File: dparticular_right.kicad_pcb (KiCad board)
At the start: 2 copper layers, 185.7 x 157.2 mm, 51 parts, among them J1 To Left Hand, SW1:10 Key_Ins, SW1:11 Key_Prnt, SW2:10 Key_F7, SW2:11 Key_F8, SW2:12 Key_F9, SW2:13 Key_F10, SW2:14 Key_F11, SW2:15 Key_F12, SW2:16 Key_Del, SW3:10 Key_7, SW3:11 Key_8, SW3:12 Key_9, SW3:13 Key_0, SW3:14 Key_Hyph, SW3:15 Key_Eql, SW3:16 Key_Bksp, SW3:9 Key_6, SW4:10 Key_U, SW4:11 Key_I, SW4:12 Key_O, SW4:13 Key_P, SW4:14 Key_LBrk, SW4:15 Key_RBrk, SW4:16 Key_BkSl, SW4:9 Key_Y, SW5:10 Key_J, SW5:11 Key_K, SW5:12 Key_L, SW5:13 Key_Semi, SW5:14 Key_Quot, SW5:16 Key_Entr, SW5:9 Key_H, SW6:10 Key_M, SW6:11 Key_Coma, SW6:12 Key_Per, SW6:13 Key_Slsh, SW6:14 Key_RShft, SW6:9 Key_N, SW7:11 Key_RAlt, SW7:12 Key_RWin, SW7:13 Key_Menu, SW7:14 Key_RCtrl, SW7:9 Key_RSpc, U1 MCP23018

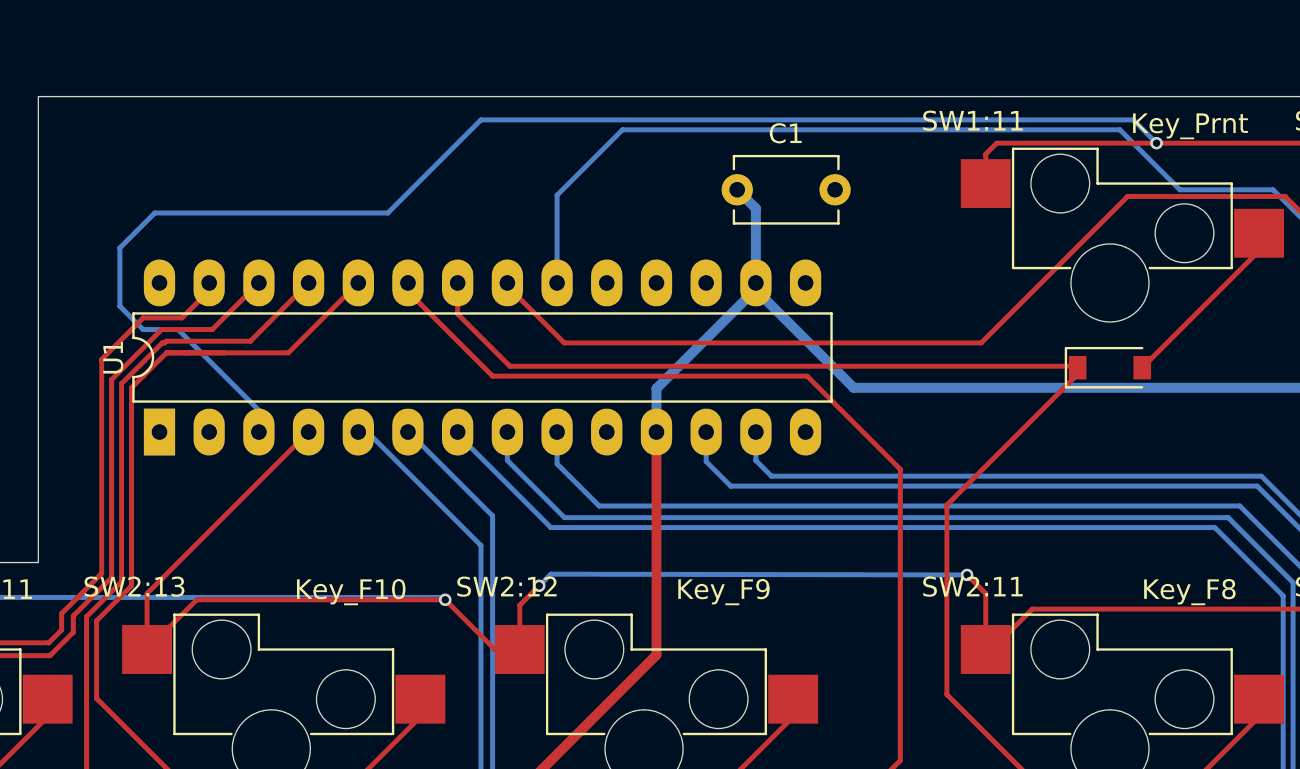
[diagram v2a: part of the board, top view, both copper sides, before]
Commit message: Righ Hand PCB: improved ground plane coverage
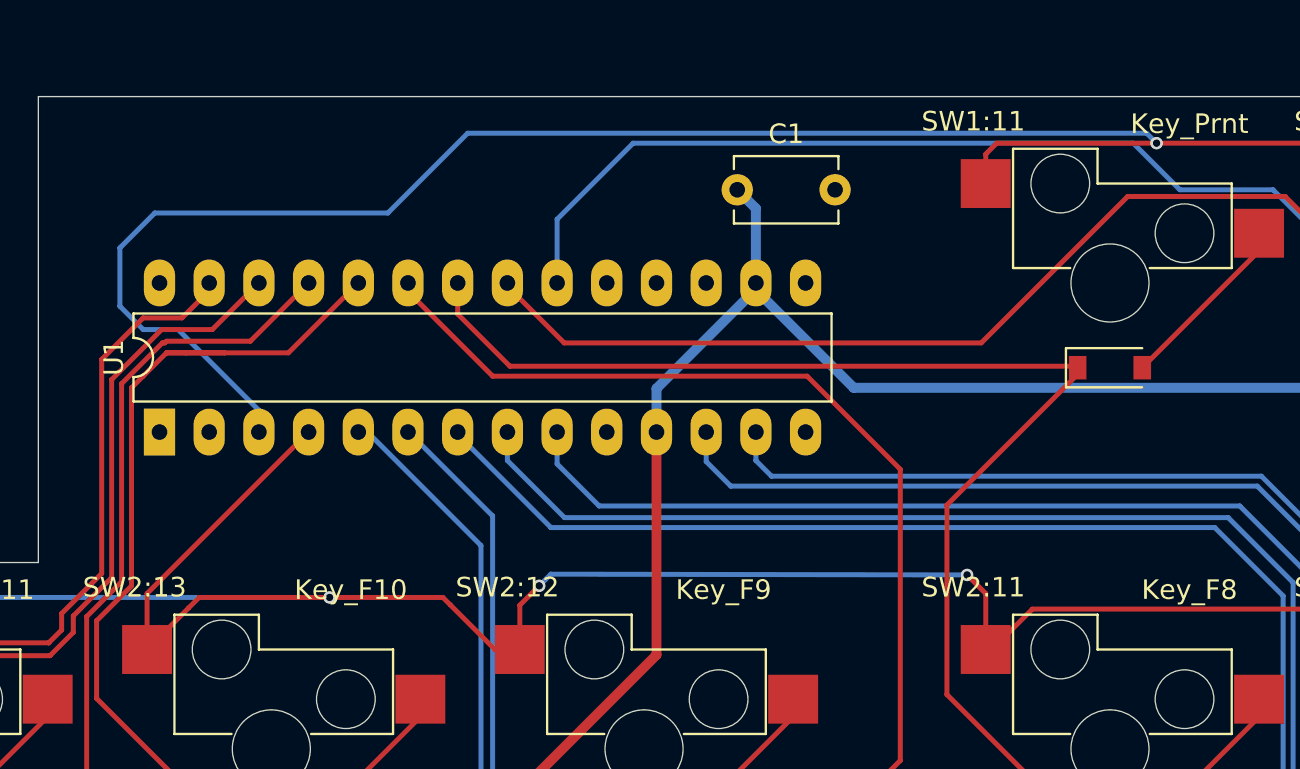
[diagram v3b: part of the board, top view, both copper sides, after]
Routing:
- net /ROW2: track 203.1 -> 197.2 mm
- net /COL9: track 254.1 -> 252.8 mm
- net /ROW1: track 91.2 -> 90.7 mm
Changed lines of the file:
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@@
     (thickness 1.6)
     (drawings 50)
-    (tracks 793)
+    (tracks 797)
     (zones 0)
     (modules 51)
@@
   (segment (start 151.37225 26.19375) (end 167.79875 26.19375) (width 0.254) (layer F.Cu) (net 11))
   (via (at 159.543852 26.19374) (size 0.635) (drill 0.381) (layers F.Cu B.Cu) (net 11))
-  (segment (start 158.353248 25.003136) (end 159.543852 26.19374) (width 0.254) (layer B.Cu) (net 11))
-  (segment (start 125.015552 25.003136) (end 158.353248 25.003136) (width 0.254) (layer B.Cu) (net 11))
-  (segment (start 120.25625 29.762438) (end 125.015552 25.003136) (width 0.254) (layer B.Cu) (net 11))
-  (segment (start 108.343622 29.762438) (end 120.25625 29.762438) (width 0.254) (layer B.Cu) (net 11))
-  (segment (start 113.665 40.9575) (end 113.665 39.846312) (width 0.254) (layer B.Cu) (net 11))
-  (segment (start 109.53744 35.718752) (end 107.751504 35.718752) (width 0.254) (layer B.Cu) (net 11))
-  (segment (start 113.665 39.846312) (end 109.53744 35.718752) (width 0.254) (layer B.Cu) (net 11))
-  (segment (start 107.751504 35.718752) (end 106.56088 34.528128) (width 0.254) (layer B.Cu) (net 11))
-  (segment (start 106.56088 34.528128) (end 106.56088 31.54518) (width 0.254) (layer B.Cu) (net 11))
-  (segment (start 106.56088 31.54518) (end 108.343622 29.762438) (width 0.254) (layer B.Cu) (net 11))
+  (segment (start 113.665 39.846312) (end 113.665 40.9575) (width 0.254) (layer B.Cu) (net 11))
+  (segment (start 109.53744 35.718752) (end 113.665 39.846312) (width 0.254) (layer B.Cu) (net 11))
+  (segment (start 107.751504 35.718752) (end 109.53744 35.718752) (width 0.254) (layer B.Cu) (net 11))
+  (segment (start 106.56088 34.528128) (end 107.751504 35.718752) (width 0.254) (layer B.Cu) (net 11))
+  (segment (start 120.25625 29.762438) (end 108.343622 29.762438) (width 0.254) (layer B.Cu) (net 11))
+  (segment (start 106.56088 31.54518) (end 106.56088 34.528128) (width 0.254) (layer B.Cu) (net 11))
+  (segment (start 159.543852 26.19374) (end 159.035862 25.68575) (width 0.254) (layer B.Cu) (net 11))
+  (segment (start 159.035862 25.68575) (end 124.332938 25.68575) (width 0.254) (layer B.Cu) (net 11))
+  (segment (start 124.332938 25.68575) (end 120.25625 29.762438) (width 0.254) (layer B.Cu) (net 11))
+  (segment (start 108.343622 29.762438) (end 106.56088 31.54518) (width 0.254) (layer B.Cu) (net 11))
   (segment (start 178.593632 151.804592) (end 180.97488 149.423344) (width 0.254) (layer F.Cu) (net 12))
   (segment (start 170.854576 151.804592) (end 178.593632 151.804592) (width 0.254) (layer F.Cu) (net 12))
@@
   (segment (start 88.9 50.8) (end 87.510947 49.410947) (width 0.254) (layer F.Cu) (net 16))
   (segment (start 116.205 40.9575) (end 115.8875 40.9575) (width 0.254) (layer B.Cu) (net 16))
-  (via (at 123.19 49.53) (size 0.635) (drill 0.381) (layers F.Cu B.Cu) (net 16))
-  (segment (start 123.070947 49.410947) (end 123.19 49.53) (width 0.254) (layer B.Cu) (net 16))
-  (segment (start 109.100947 49.410947) (end 123.070947 49.410947) (width 0.254) (layer B.Cu) (net 16))
   (segment (start 109.100947 49.410947) (end 71.239053 49.410947) (width 0.254) (layer B.Cu) (net 16))
   (segment (start 125.73 52.07) (end 127 52.07) (width 0.254) (layer F.Cu) (net 16))
-  (segment (start 123.19 49.53) (end 125.73 52.07) (width 0.254) (layer F.Cu) (net 16))
-  (segment (start 107.95 52.07) (end 110.49 49.53) (width 0.254) (layer F.Cu) (net 16))
-  (segment (start 110.49 49.53) (end 123.19 49.53) (width 0.254) (layer F.Cu) (net 16))
+  (segment (start 113.109293 49.410947) (end 117.276477 49.410947) (width 0.254) (layer B.Cu) (net 16))
+  (segment (start 117.276477 49.410947) (end 117.276496 49.410928) (width 0.254) (layer B.Cu) (net 16))
+  (via (at 117.276496 49.410928) (size 0.635) (drill 0.381) (layers F.Cu B.Cu) (net 16))
+  (segment (start 109.100947 49.410947) (end 113.109293 49.410947) (width 0.254) (layer B.Cu) (net 16))
+  (segment (start 123.070928 49.410928) (end 123.447928 49.787928) (width 0.254) (layer F.Cu) (net 16))
+  (segment (start 117.276496 49.410928) (end 123.070928 49.410928) (width 0.254) (layer F.Cu) (net 16))
+  (segment (start 123.447928 49.787928) (end 125.73 52.07) (width 0.254) (layer F.Cu) (net 16))
+  (segment (start 110.609072 49.410928) (end 110.073256 49.946744) (width 0.254) (layer F.Cu) (net 16))
+  (segment (start 107.95 52.07) (end 110.073256 49.946744) (width 0.254) (layer F.Cu) (net 16))
+  (segment (start 117.276496 49.410928) (end 110.609072 49.410928) (width 0.254) (layer F.Cu) (net 16))
   (segment (start 164.7825 55.51022) (end 158.81186 61.48086) (width 0.254) (layer F.Cu) (net 17))
   (segment (start 164.7825 54.61) (end 164.7825 55.51022) (width 0.254) (layer F.Cu) (net 17))
@@
   (segment (start 198.12 87.9475) (end 198.12 88.84772) (width 0.254) (layer F.Cu) (net 27))
   (segment (start 186.76428 94.81836) (end 188.84936 94.81836) (width 0.254) (layer F.Cu) (net 28))
-  (segment (start 128.905 33.3375) (end 128.905 28.852744) (width 0.254) (layer B.Cu) (net 28))
-  (segment (start 132.246598 25.511146) (end 157.67041 25.511146) (width 0.254) (layer B.Cu) (net 28))
-  (segment (start 128.905 28.852744) (end 132.246598 25.511146) (width 0.254) (layer B.Cu) (net 28))
-  (segment (start 157.67041 25.511146) (end 160.734272 28.575008) (width 0.254) (layer B.Cu) (net 28))
   (segment (start 179.928415 36.393471) (end 185.142064 41.60712) (width 0.254) (layer B.Cu) (net 28))
   (segment (start 173.315231 36.393471) (end 179.928415 36.393471) (width 0.254) (layer B.Cu) (net 28))
-  (segment (start 160.734272 28.575008) (end 165.496768 28.575008) (width 0.254) (layer B.Cu) (net 28))
   (segment (start 172.342856 35.421096) (end 173.315231 36.393471) (width 0.254) (layer B.Cu) (net 28))
-  (segment (start 165.496768 28.575008) (end 172.342856 35.421096) (width 0.254) (layer B.Cu) (net 28))
   (segment (start 186.76428 90.055864) (end 186.76428 94.81836) (width 0.254) (layer B.Cu) (net 28))
   (segment (start 190.499872 69.651536) (end 190.499872 86.320272) (width 0.254) (layer B.Cu) (net 28))
@@
   (segment (start 182.165504 156.567088) (end 179.784256 158.948336) (width 0.254) (layer F.Cu) (net 28))
   (segment (start 179.784256 169.097006) (end 179.784256 161.329584) (width 0.254) (layer F.Cu) (net 28))
+  (segment (start 160.734272 28.575008) (end 165.496768 28.575008) (width 0.254) (layer B.Cu) (net 28))
+  (segment (start 165.496768 28.575008) (end 172.342856 35.421096) (width 0.254) (layer B.Cu) (net 28))
+  (segment (start 132.794448 26.19376) (end 158.353024 26.19376) (width 0.254) (layer B.Cu) (net 28))
+  (segment (start 128.905 30.083208) (end 132.794448 26.19376) (width 0.254) (layer B.Cu) (net 28))
+  (segment (start 158.353024 26.19376) (end 160.734272 28.575008) (width 0.254) (layer B.Cu) (net 28))
+  (segment (start 128.905 33.3375) (end 128.905 30.083208) (width 0.254) (layer B.Cu) (net 28))
   (segment (start 69.85 83.9035) (end 70.40975 83.34375) (width 0.254) (layer F.Cu) (net 29))
   (segment (start 69.85 85.4075) (end 69.85 83.9035) (width 0.254) (layer F.Cu) (net 29))

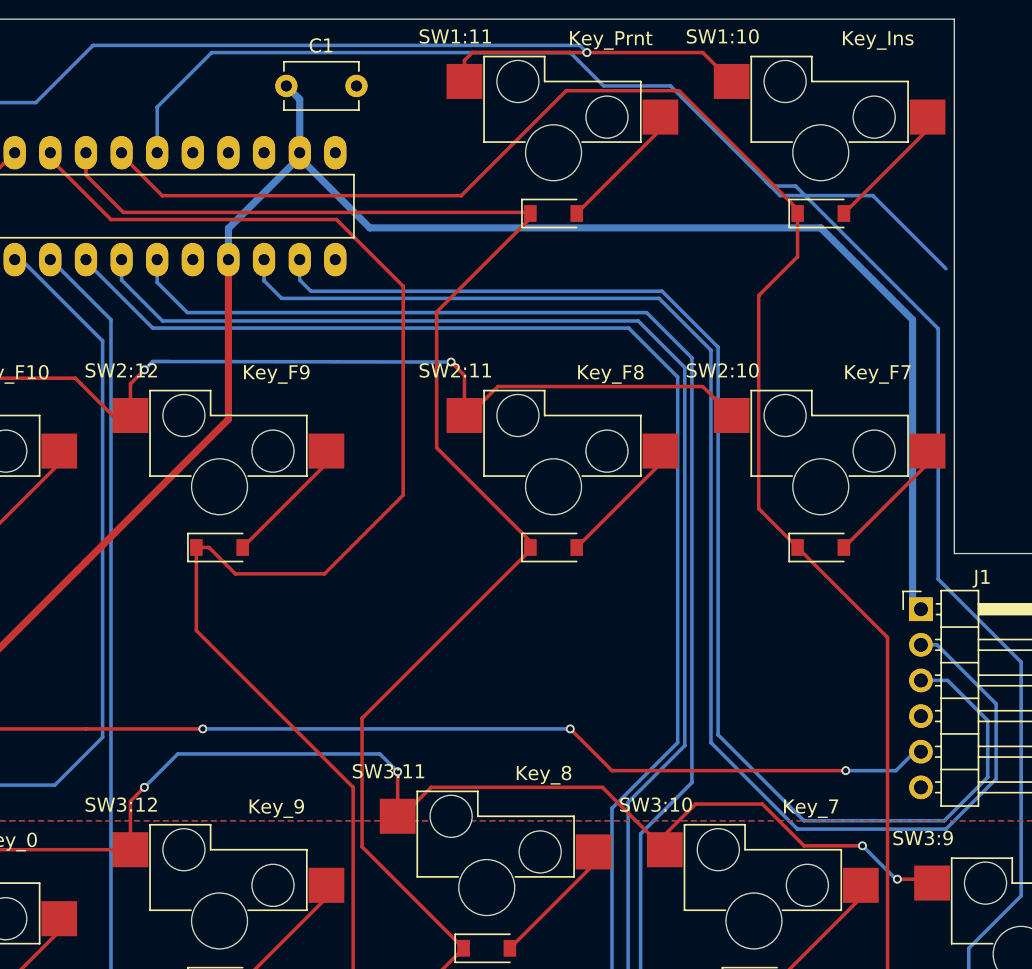
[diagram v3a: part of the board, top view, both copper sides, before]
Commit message: Right Hand PCB: Tidying and ground fill expanding
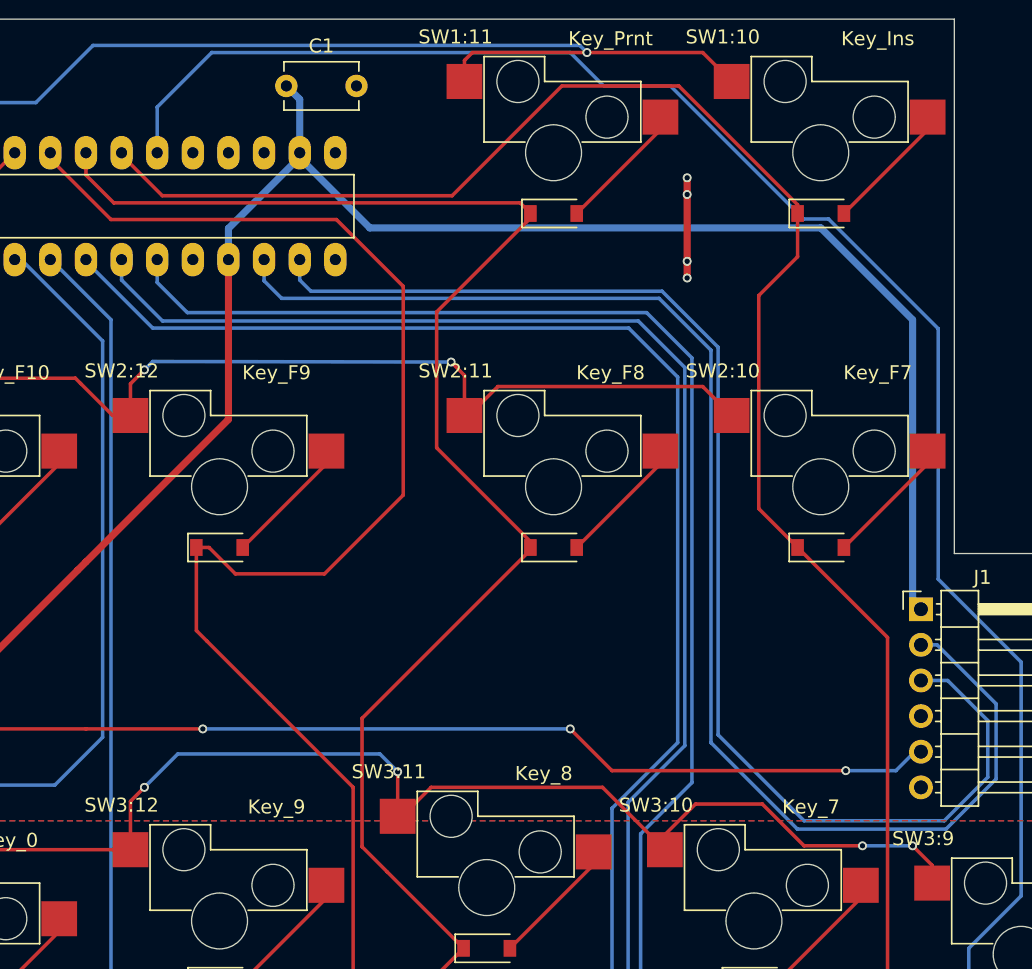
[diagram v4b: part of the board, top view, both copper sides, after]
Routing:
- net /COL9: track 252.8 -> 237.5 mm
- net GND: track 40.7 -> 47.8 mm, vias 0 -> 4
- net /ROW3: track 248.2 -> 249.0 mm
